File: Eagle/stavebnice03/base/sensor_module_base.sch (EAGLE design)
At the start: 19 parts

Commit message: C0603 changed to C0603K with wider space between soldering areas
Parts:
- C1, C2, C3, C4, C5: device resistor:C-EUC0603 -> resistor:C-EUC0603K
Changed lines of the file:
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@@
 <parts>
 <part name="U$1" library="!stavebnice03" deviceset="16F103-TSSOP" device=""/>
-<part name="C2" library="resistor" deviceset="C-EU" device="C0603" value="100nF"/>
+<part name="C2" library="resistor" deviceset="C-EU" device="C0603K" value="100nF"/>
 <part name="R1" library="resistor" deviceset="R-EU_" device="R0603" value="2k2"/>
 <part name="R2" library="resistor" deviceset="R-EU_" device="R0603" value="2k2"/>
 <part name="U$2" library="!stavebnice03" deviceset="NC7SB3157P6X" device=""/>
 <part name="U$3" library="!stavebnice03" deviceset="NC7SB3157P6X" device=""/>
-<part name="C1" library="resistor" deviceset="C-EU" device="C0603" value="100nF"/>
-<part name="C3" library="resistor" deviceset="C-EU" device="C0603" value="100nF"/>
+<part name="C1" library="resistor" deviceset="C-EU" device="C0603K" value="100nF"/>
+<part name="C3" library="resistor" deviceset="C-EU" device="C0603K" value="100nF"/>
 <part name="U$4" library="!stavebnice03" deviceset="JUMPER5M-90" device=""/>
 <part name="U$5" library="!stavebnice03" deviceset="JUMPER5F-90" device=""/>
 <part name="U$6" library="!stavebnice03" deviceset="NC7SB3157P6X" device=""/>
 <part name="U$7" library="!stavebnice03" deviceset="NC7SB3157P6X" device=""/>
-<part name="C5" library="resistor" deviceset="C-EU" device="C0603" value="100nF"/>
-<part name="C4" library="resistor" deviceset="C-EU" device="C0603" value="100nF"/>
+<part name="C5" library="resistor" deviceset="C-EU" device="C0603K" value="100nF"/>
+<part name="C4" library="resistor" deviceset="C-EU" device="C0603K" value="100nF"/>
 <part name="U$9" library="!stavebnice03" deviceset="JUMPER4M" device=""/>
 <part name="R3" library="resistor" deviceset="R-EU_" device="R0603" value="2K2"/>

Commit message: layer coloring and place drawing moved to docu layer + changed sizes of names and values
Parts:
- renumbered U$1 to U1, U$2 to U2, U$3 to U3, U$4 to IN, U$5 to OUT, U$6 to U4, U$7 to U5, U$8 to PROG, U$9 to DATA

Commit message: eagle adjustment for the Jíťa version
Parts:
- U1: value 16F103-TSSOP -> 16F103
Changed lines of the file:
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@@
 <layer number="19" name="Unrouted" color="6" fill="1" visible="no" active="no"/>
 <layer number="20" name="Dimension" color="15" fill="1" visible="no" active="no"/>
-<layer number="21" name="tPlace" color="7" fill="1" visible="no" active="no"/>
-<layer number="22" name="bPlace" color="7" fill="1" visible="no" active="no"/>
+<layer number="21" name="tPlace" color="14" fill="1" visible="no" active="no"/>
+<layer number="22" name="bPlace" color="14" fill="1" visible="no" active="no"/>
 <layer number="23" name="tOrigins" color="15" fill="1" visible="no" active="no"/>
 <layer number="24" name="bOrigins" color="15" fill="1" visible="no" active="no"/>
-<layer number="25" name="tNames" color="7" fill="1" visible="no" active="no"/>
-<layer number="26" name="bNames" color="7" fill="1" visible="no" active="no"/>
-<layer number="27" name="tValues" color="7" fill="1" visible="no" active="no"/>
-<layer number="28" name="bValues" color="7" fill="1" visible="no" active="no"/>
+<layer number="25" name="tNames" color="3" fill="1" visible="no" active="no"/>
+<layer number="26" name="bNames" color="6" fill="1" visible="no" active="no"/>
+<layer number="27" name="tValues" color="11" fill="1" visible="no" active="no"/>
+<layer number="28" name="bValues" color="11" fill="1" visible="no" active="no"/>
 <layer number="29" name="tStop" color="7" fill="3" visible="no" active="no"/>
 <layer number="30" name="bStop" color="7" fill="6" visible="no" active="no"/>
@@
 </classes>
 <parts>
-<part name="U1" library="!stavebnice03" deviceset="16F103-TSSOP" device=""/>
+<part name="U1" library="!stavebnice03" deviceset="16F103-TSSOP" device="" value="16F103"/>
 <part name="C2" library="resistor" deviceset="C-EU" device="C0603K" value="100nF"/>
 <part name="R1" library="resistor" deviceset="R-EU_" device="R0603" value="2k2"/>
 <part name="R2" library="resistor" deviceset="R-EU_" device="R0603" value="2k2"/>
-<part name="U2" library="!stavebnice03" deviceset="NC7SB3157P6X" device=""/>
-<part name="U3" library="!stavebnice03" deviceset="NC7SB3157P6X" device=""/>
+<part name="U2" library="!stavebnice03" deviceset="NC7SB3157P6X" device="" value=""/>
+<part name="U3" library="!stavebnice03" deviceset="NC7SB3157P6X" device="" value=""/>
 <part name="C1" library="resistor" deviceset="C-EU" device="C0603K" value="100nF"/>
 <part name="C3" library="resistor" deviceset="C-EU" device="C0603K" value="100nF"/>
-<part name="IN" library="!stavebnice03" deviceset="JUMPER5M-90" device=""/>
-<part name="OUT" library="!stavebnice03" deviceset="JUMPER5F-90" device=""/>
-<part name="U4" library="!stavebnice03" deviceset="NC7SB3157P6X" device=""/>
-<part name="U5" library="!stavebnice03" deviceset="NC7SB3157P6X" device=""/>
+<part name="IN" library="!stavebnice03" deviceset="JUMPER5M-90" device="" value=""/>
+<part name="OUT" library="!stavebnice03" deviceset="JUMPER5F-90" device="" value=""/>
+<part name="U4" library="!stavebnice03" deviceset="NC7SB3157P6X" device="" value=""/>
+<part name="U5" library="!stavebnice03" deviceset="NC7SB3157P6X" device="" value=""/>
 <part name="C5" library="resistor" deviceset="C-EU" device="C0603K" value="100nF"/>
 <part name="C4" library="resistor" deviceset="C-EU" device="C0603K" value="100nF"/>
-<part name="DATA" library="!stavebnice03" deviceset="JUMPER4M" device=""/>
+<part name="DATA" library="!stavebnice03" deviceset="JUMPER4M" device="" value="JUMPER4M"/>
 <part name="R3" library="resistor" deviceset="R-EU_" device="R0603" value="2K2"/>
 <part name="R4" library="resistor" deviceset="R-EU_" device="R0603" value="2k2"/>
 <part name="R5" library="resistor" deviceset="R-EU_" device="R0603" value="100k"/>
-<part name="PROG" library="!stavebnice03" deviceset="JUMPER5M" device=""/>
+<part name="PROG" library="!stavebnice03" deviceset="JUMPER5M" device="" value="JUMPER5M"/>
 </parts>
 <sheets>
@@
 <net name="N$13" class="0">
 <segment>
-<wire x1="162.56" y1="50.8" x2="162.56" y2="53.34" width="0.1524" layer="91"/>
+<wire x1="162.56" y1="50.8" x2="162.56" y2="53.34" width="0.1524" layer="91" style="dashdot"/>
 <wire x1="162.56" y1="53.34" x2="106.68" y2="53.34" width="0.1524" layer="91"/>
 <wire x1="106.68" y1="53.34" x2="106.68" y2="83.82" width="0.1524" layer="91"/>

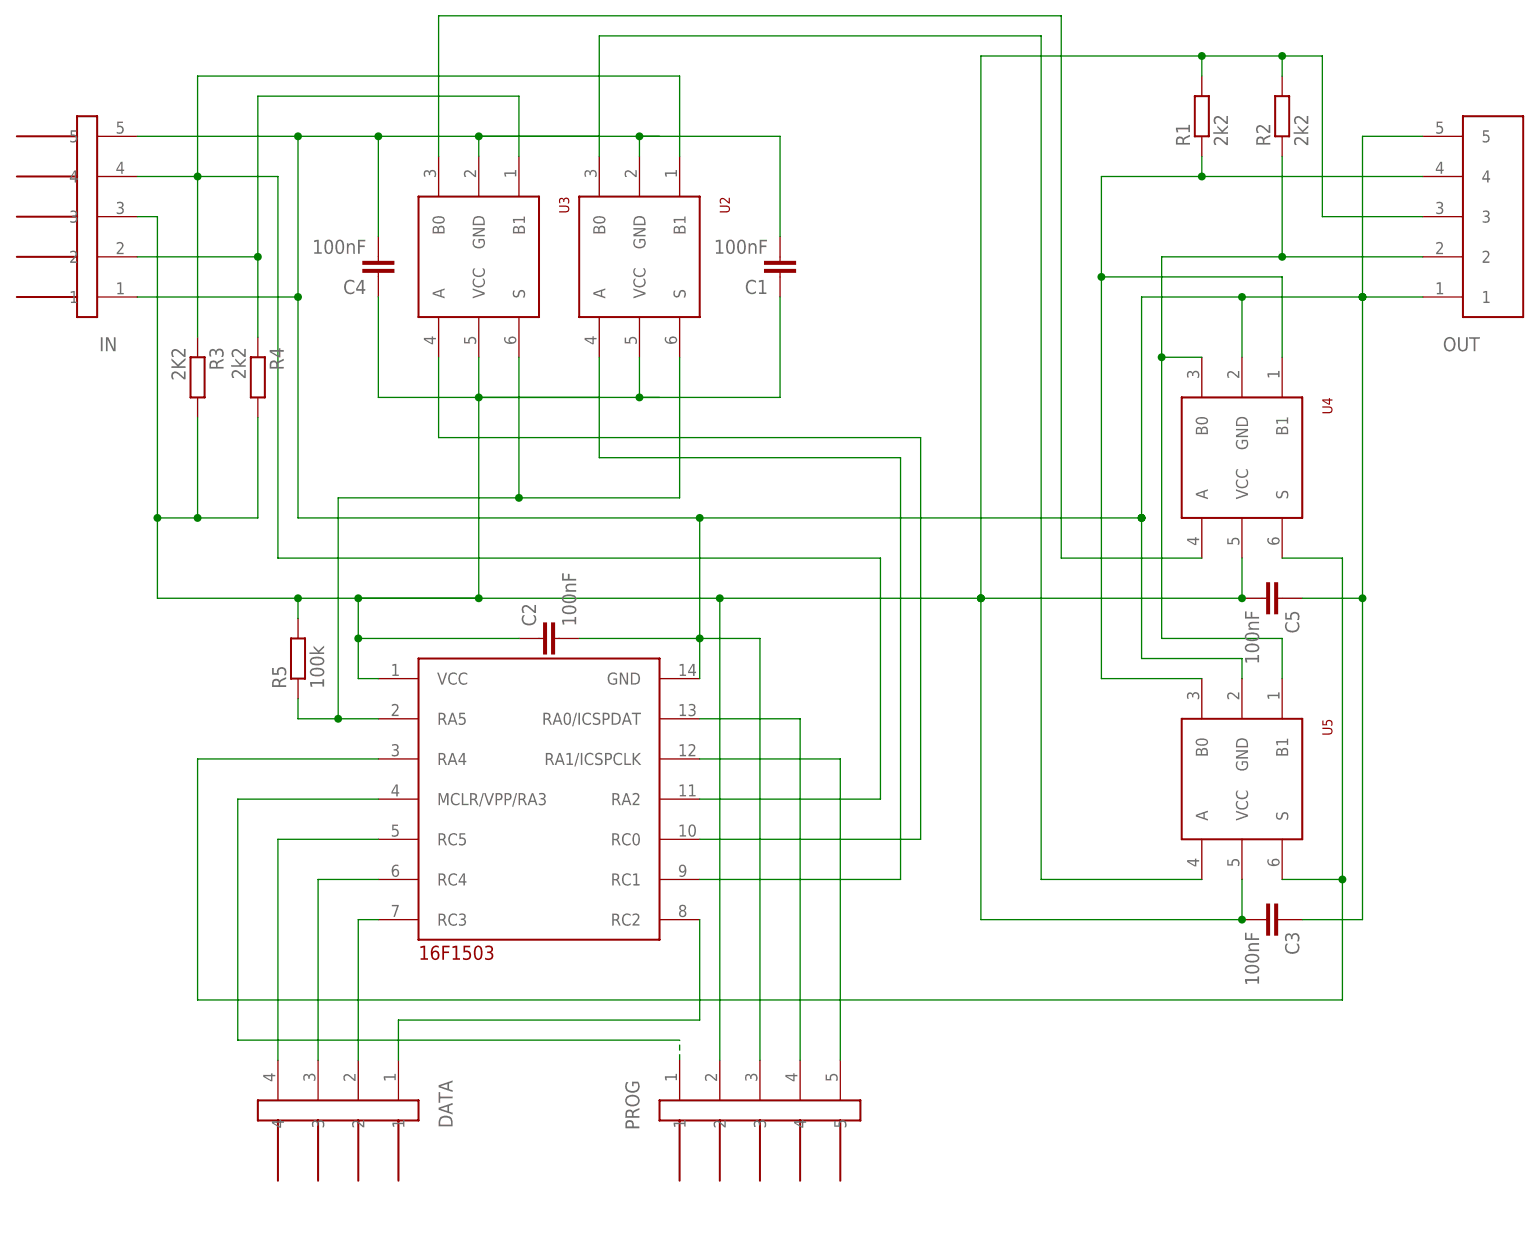
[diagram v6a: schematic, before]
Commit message: changes for pcb making by a seed studio
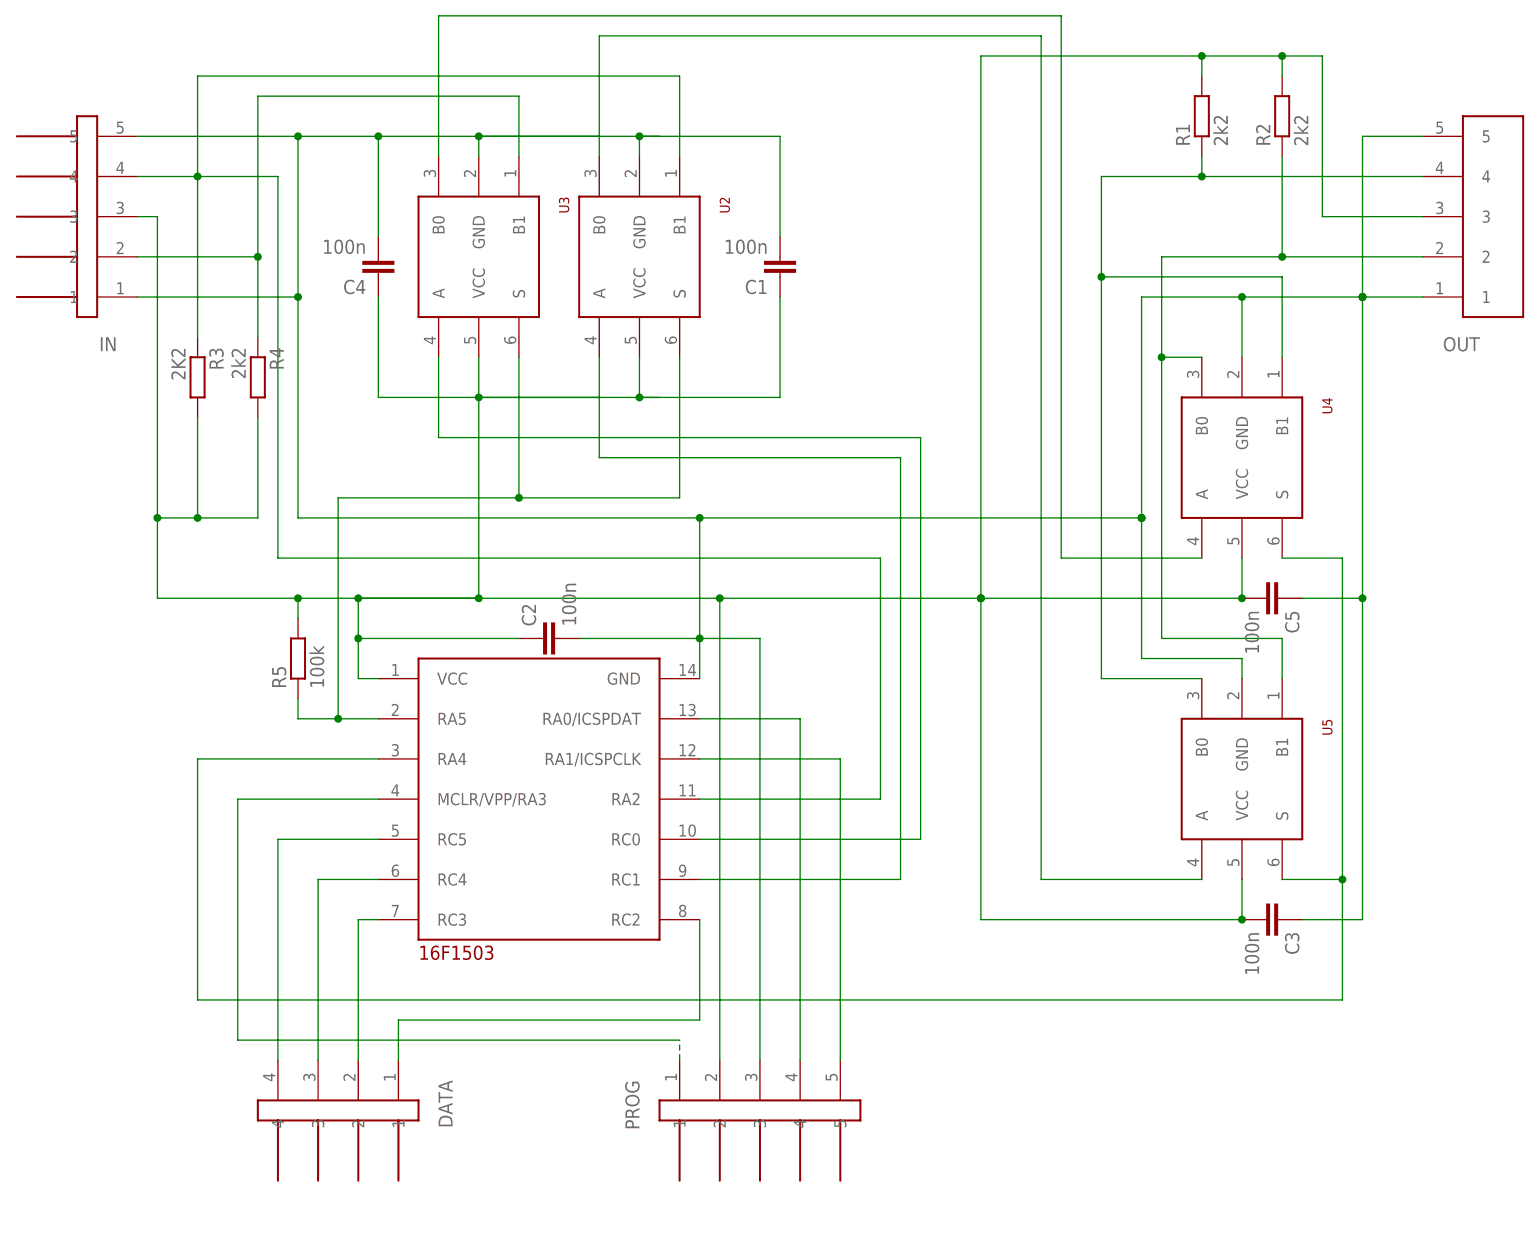
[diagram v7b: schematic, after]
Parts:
- C1, C2, C3, C4, C5: value 100nF -> 100n
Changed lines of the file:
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@@
 <parts>
 <part name="U1" library="!stavebnice03" deviceset="16F103-TSSOP" device="" value="16F103"/>
-<part name="C2" library="resistor" deviceset="C-EU" device="C0603K" value="100nF"/>
+<part name="C2" library="resistor" deviceset="C-EU" device="C0603K" value="100n"/>
 <part name="R1" library="resistor" deviceset="R-EU_" device="R0603" value="2k2"/>
 <part name="R2" library="resistor" deviceset="R-EU_" device="R0603" value="2k2"/>
 <part name="U2" library="!stavebnice03" deviceset="NC7SB3157P6X" device="" value=""/>
 <part name="U3" library="!stavebnice03" deviceset="NC7SB3157P6X" device="" value=""/>
-<part name="C1" library="resistor" deviceset="C-EU" device="C0603K" value="100nF"/>
-<part name="C3" library="resistor" deviceset="C-EU" device="C0603K" value="100nF"/>
-<part name="IN" library="!stavebnice03" deviceset="JUMPER5M-90" device="" value=""/>
-<part name="OUT" library="!stavebnice03" deviceset="JUMPER5F-90" device="" value=""/>
+<part name="C1" library="resistor" deviceset="C-EU" device="C0603K" value="100n"/>
+<part name="C3" library="resistor" deviceset="C-EU" device="C0603K" value="100n"/>
+<part name="IN" library="!stavebnice03" deviceset="JUMPER5M-90" device="" value="JUMPER5M-90"/>
+<part name="OUT" library="!stavebnice03" deviceset="JUMPER5F-90" device="" value="JUMPER5F-90"/>
 <part name="U4" library="!stavebnice03" deviceset="NC7SB3157P6X" device="" value=""/>
 <part name="U5" library="!stavebnice03" deviceset="NC7SB3157P6X" device="" value=""/>
-<part name="C5" library="resistor" deviceset="C-EU" device="C0603K" value="100nF"/>
-<part name="C4" library="resistor" deviceset="C-EU" device="C0603K" value="100nF"/>
+<part name="C5" library="resistor" deviceset="C-EU" device="C0603K" value="100n"/>
+<part name="C4" library="resistor" deviceset="C-EU" device="C0603K" value="100n"/>
 <part name="DATA" library="!stavebnice03" deviceset="JUMPER4M" device="" value="JUMPER4M"/>
 <part name="R3" library="resistor" deviceset="R-EU_" device="R0603" value="2K2"/>
